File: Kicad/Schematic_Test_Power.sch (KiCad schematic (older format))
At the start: 16 parts, among them J201 Conn_02x01 BATTERY, SW201 SW_DIP_x01, U201 STBC08, U202 AP22811BW5, U203 TLV75528PDBV

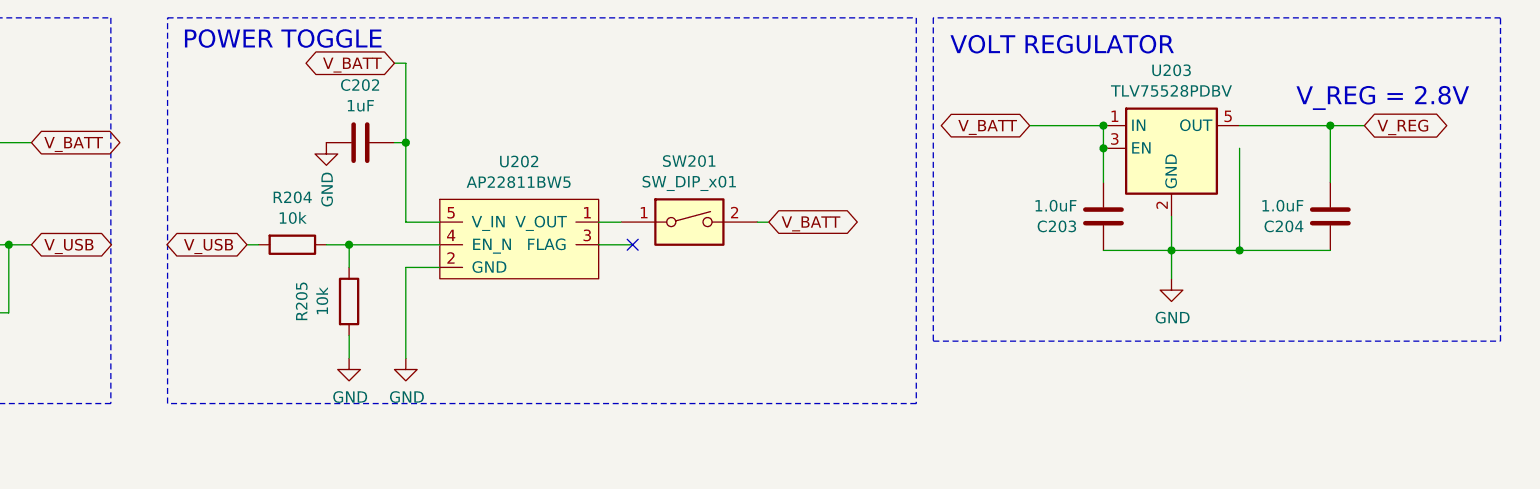
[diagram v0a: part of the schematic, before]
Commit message: Corrected some schematic labeling.
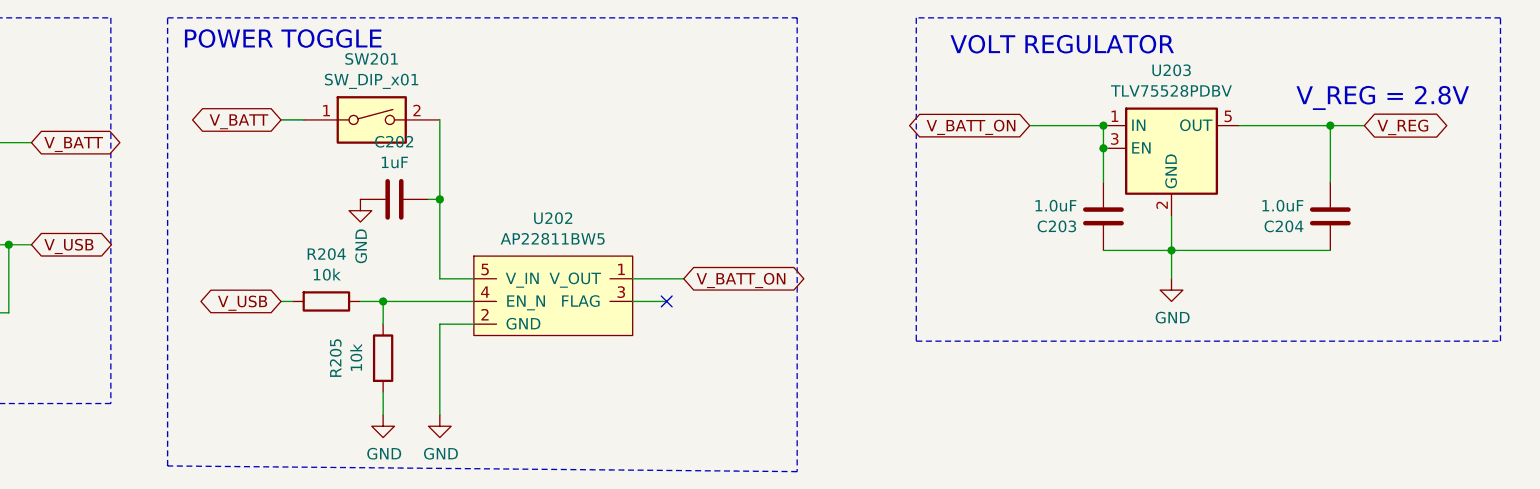
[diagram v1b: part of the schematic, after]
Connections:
- net GND: no longer U203.4 (NC)
- net V_BATT: now also SW201.1; no longer C202.1, C203.2, SW201.2, U202.5 (V_IN), U203.1 (IN), U203.3 (EN)
- net V_BATT_ON: now reaches U202.1 (V_OUT)
- net V_BATT_ON: now also C203.2, U203.1 (IN), U203.3 (EN); no longer SW201.1
- new net: C202.1, SW201.2, U202.5 (V_IN)
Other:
- moved on the sheet: C202, R204, R205, SW201, U202
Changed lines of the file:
@@
 L power:GND #PWR?
 U 1 1 5F6E4B62
-P 5725 3725
+P 5875 3975
 AR Path="/5F6E4B62" Ref="#PWR?"  Part="1"
 AR Path="/5F580D08/5F6E4B62" Ref="#PWR0207"  Part="1"
-F 0 "#PWR0207" H 5725 3475 50  0001 C CNN
-F 1 "GND" H 5730 3552 50  0000 C CNN
-F 2 "" H 5725 3725 50  0001 C CNN
-F 3 "" H 5725 3725 50  0001 C CNN
-	1    5725 3725
-	1    0    0    -1
-$EndComp
-Wire Wire Line
-	5725 3325 5725 3725
-Wire Wire Line
-	5875 3325 5725 3325
-Text GLabel 5675 2425 0    50   BiDi ~ 0
-V_BATT
+F 0 "#PWR0207" H 5875 3725 50  0001 C CNN
+F 1 "GND" H 5880 3802 50  0000 C CNN
+F 2 "" H 5875 3975 50  0001 C CNN
+F 3 "" H 5875 3975 50  0001 C CNN
+	1    5875 3975
+	1    0    0    -1
+$EndComp
+Wire Wire Line
+	5875 3575 5875 3975
+Wire Wire Line
+	6025 3575 5875 3575
 $Comp
 L StarGazer:AP22811BW5 U?
 U 1 1 5F6E4B6E
-P 6225 3025
+P 6375 3275
 AR Path="/5F6E4B6E" Ref="U?"  Part="1"
 AR Path="/5F580D08/5F6E4B6E" Ref="U202"  Part="1"
-F 0 "U202" H 6225 3190 50  0000 C CNN
-F 1 "AP22811BW5" H 6225 3099 50  0000 C CNN
-F 2 "Package_TO_SOT_SMD:TSOT-23-5_HandSoldering" H 6225 3075 50  0001 C CNN
-F 3 "" H 6225 3075 50  0001 C CNN
-F 4 "Mosfet, active low (batt protection)" H 6225 3025 50  0001 C CNN "part_details"
-F 5 " AP22811BW5-7 " H 6225 3025 50  0001 C CNN "part_name"
-F 6 "https://www.digikey.com/product-detail/en/diodes-incorporated/AP22811BW5-7/AP22811BW5-7DICT-ND/8545787" H 6225 3025 50  0001 C CNN "part_url"
-	1    6225 3025
+F 0 "U202" H 6375 3440 50  0000 C CNN
+F 1 "AP22811BW5" H 6375 3349 50  0000 C CNN
+F 2 "Package_TO_SOT_SMD:TSOT-23-5_HandSoldering" H 6375 3325 50  0001 C CNN
+F 3 "" H 6375 3325 50  0001 C CNN
+F 4 "Mosfet, active low (batt protection)" H 6375 3275 50  0001 C CNN "part_details"
+F 5 " AP22811BW5-7 " H 6375 3275 50  0001 C CNN "part_name"
+F 6 "https://www.digikey.com/product-detail/en/diodes-incorporated/AP22811BW5-7/AP22811BW5-7DICT-ND/8545787" H 6375 3275 50  0001 C CNN "part_url"
+	1    6375 3275
 	1    0    0    -1
 $EndComp
@@
 L Device:C C?
 U 1 1 5F6E4B74
-P 5525 2775
+P 5675 3025
 AR Path="/5F6E4B74" Ref="C?"  Part="1"
 AR Path="/5F580D08/5F6E4B74" Ref="C202"  Part="1"
-F 0 "C202" V 5273 2775 50  0000 C CNN
-F 1 "1uF" V 5364 2775 50  0000 C CNN
-F 2 "" H 5563 2625 50  0001 C CNN
-F 3 "~" H 5525 2775 50  0001 C CNN
-	1    5525 2775
+F 0 "C202" V 5423 3025 50  0000 C CNN
+F 1 "1uF" V 5514 3025 50  0000 C CNN
+F 2 "" H 5713 2875 50  0001 C CNN
+F 3 "~" H 5675 3025 50  0001 C CNN
+	1    5675 3025
 	0    1    1    0
 $EndComp
@@
 L power:GND #PWR?
 U 1 1 5F6E4B7A
-P 5375 2775
+P 5525 3025
 AR Path="/5F6E4B7A" Ref="#PWR?"  Part="1"
 AR Path="/5F580D08/5F6E4B7A" Ref="#PWR0205"  Part="1"
-F 0 "#PWR0205" H 5375 2525 50  0001 C CNN
-F 1 "GND" V 5380 2647 50  0000 R CNN
-F 2 "" H 5375 2775 50  0001 C CNN
-F 3 "" H 5375 2775 50  0001 C CNN
-	1    5375 2775
+F 0 "#PWR0205" H 5525 2775 50  0001 C CNN
+F 1 "GND" V 5530 2897 50  0000 R CNN
+F 2 "" H 5525 3025 50  0001 C CNN
+F 3 "" H 5525 3025 50  0001 C CNN
+	1    5525 3025
 	1    0    0    -1
 $EndComp
@@
 L Device:R R?
 U 1 1 5F6E4B84
-P 5475 3475
+P 5625 3725
 AR Path="/5F6E4B84" Ref="R?"  Part="1"
 AR Path="/5F580D08/5F6E4B84" Ref="R205"  Part="1"
-F 0 "R205" V 5268 3475 50  0000 C CNN
-F 1 "10k" V 5359 3475 50  0000 C CNN
-F 2 "Resistor_SMD:R_1206_3216Metric_Pad1.42x1.75mm_HandSolder" V 5405 3475 50  0001 C CNN
-F 3 "~" H 5475 3475 50  0001 C CNN
-F 4 "" H 5475 3475 50  0001 C CNN "Name"
-F 5 "" H 5475 3475 50  0001 C CNN "part_details"
-F 6 "Resistor - Pull Up" H 5475 3475 50  0001 C CNN "part_name"
-F 7 "https://www.digikey.com/product-detail/en/yageo/RC1206JR-0710KL/311-10KERCT-ND/732156" H 5475 3475 50  0001 C CNN "part_url"
-	1    5475 3475
-	1    0    0    -1
-$EndComp
-Wire Wire Line
-	5475 3625 5475 3725
+F 0 "R205" V 5418 3725 50  0000 C CNN
+F 1 "10k" V 5509 3725 50  0000 C CNN
+F 2 "Resistor_SMD:R_1206_3216Metric_Pad1.42x1.75mm_HandSolder" V 5555 3725 50  0001 C CNN
+F 3 "~" H 5625 3725 50  0001 C CNN
+F 4 "" H 5625 3725 50  0001 C CNN "Name"
+F 5 "" H 5625 3725 50  0001 C CNN "part_details"
+F 6 "Resistor - Pull Up" H 5625 3725 50  0001 C CNN "part_name"
+F 7 "https://www.digikey.com/product-detail/en/yageo/RC1206JR-0710KL/311-10KERCT-ND/732156" H 5625 3725 50  0001 C CNN "part_url"
+	1    5625 3725
+	1    0    0    -1
+$EndComp
+Wire Wire Line
+	5625 3875 5625 3975
 $Comp
 L power:GND #PWR?
 U 1 1 5F6E4B8B
-P 5475 3725
+P 5625 3975
 AR Path="/5F6E4B8B" Ref="#PWR?"  Part="1"
 AR Path="/5F580D08/5F6E4B8B" Ref="#PWR0206"  Part="1"
-F 0 "#PWR0206" H 5475 3475 50  0001 C CNN
-F 1 "GND" H 5480 3552 50  0000 C CNN
-F 2 "" H 5475 3725 50  0001 C CNN
-F 3 "" H 5475 3725 50  0001 C CNN
-	1    5475 3725
-	1    0    0    -1
-$EndComp
-Wire Wire Line
-	5475 3325 5475 3225
-Wire Wire Line
-	5475 3225 5875 3225
-Connection ~ 5475 3225
-Text GLabel 5025 3225 0    50   BiDi ~ 0
+F 0 "#PWR0206" H 5625 3725 50  0001 C CNN
+F 1 "GND" H 5630 3802 50  0000 C CNN
+F 2 "" H 5625 3975 50  0001 C CNN
+F 3 "" H 5625 3975 50  0001 C CNN
+	1    5625 3975
+	1    0    0    -1
+$EndComp
+Wire Wire Line
+	5625 3575 5625 3475
+Wire Wire Line
+	5625 3475 6025 3475
+Connection ~ 5625 3475
+Text GLabel 5175 3475 0    50   BiDi ~ 0
 V_USB
 Wire Wire Line
-	5075 3225 5025 3225
-Wire Wire Line
-	5375 3225 5475 3225
+	5225 3475 5175 3475
+Wire Wire Line
+	5525 3475 5625 3475
 $Comp
 L Device:R R?
 U 1 1 5F6E4B9B
-P 5225 3225
+P 5375 3475
 AR Path="/5F6E4B9B" Ref="R?"  Part="1"
 AR Path="/5F580D08/5F6E4B9B" Ref="R204"  Part="1"
-F 0 "R204" V 5018 3225 50  0000 C CNN
-F 1 "10k" V 5109 3225 50  0000 C CNN
-F 2 "Resistor_SMD:R_1206_3216Metric_Pad1.42x1.75mm_HandSolder" V 5155 3225 50  0001 C CNN
-F 3 "~" H 5225 3225 50  0001 C CNN
-F 4 "" H 5225 3225 50  0001 C CNN "Name"
-F 5 "" H 5225 3225 50  0001 C CNN "part_details"
-F 6 "Resistor - Pull Up" H 5225 3225 50  0001 C CNN "part_name"
-F 7 "https://www.digikey.com/product-detail/en/yageo/RC1206JR-0710KL/311-10KERCT-ND/732156" H 5225 3225 50  0001 C CNN "part_url"
-	1    5225 3225
+F 0 "R204" V 5168 3475 50  0000 C CNN
+F 1 "10k" V 5259 3475 50  0000 C CNN
+F 2 "Resistor_SMD:R_1206_3216Metric_Pad1.42x1.75mm_HandSolder" V 5305 3475 50  0001 C CNN
+F 3 "~" H 5375 3475 50  0001 C CNN
+F 4 "" H 5375 3475 50  0001 C CNN "Name"
+F 5 "" H 5375 3475 50  0001 C CNN "part_details"
+F 6 "Resistor - Pull Up" H 5375 3475 50  0001 C CNN "part_name"
+F 7 "https://www.digikey.com/product-detail/en/yageo/RC1206JR-0710KL/311-10KERCT-ND/732156" H 5375 3475 50  0001 C CNN "part_url"
+	1    5375 3475
 	0    1    1    0
 $EndComp
 Wire Wire Line
-	5725 3125 5875 3125
-Wire Wire Line
-	6575 3225 6725 3225
+	5875 3375 6025 3375
+Wire Wire Line
+	6725 3475 6875 3475
 Connection ~ 3075 2775
 Text Notes 3625 3775 2    50   ~ 0
@@
 Wire Notes Line
 	4425 3925 875  3925
-NoConn ~ 6725 3225
-Wire Wire Line
-	5675 2775 5725 2775
-Wire Wire Line
-	5725 2775 5725 3125
-Connection ~ 5725 2775
-Wire Wire Line
-	5725 2775 5725 2425
-Wire Wire Line
-	5725 2425 5675 2425
-Wire Notes Line
-	4675 3925 4675 2225
-Wire Notes Line
-	4675 2225 7975 2225
-Wire Notes Line
-	7975 2225 7975 3925
-Wire Notes Line
-	7975 3925 4675 3925
+NoConn ~ 6875 3475
+Wire Wire Line
+	5825 3025 5875 3025
+Wire Wire Line
+	5875 3025 5875 3375
+Connection ~ 5875 3025
+Wire Wire Line
+	5875 3025 5875 2675
+Wire Notes Line
+	4675 4200 4675 2225
+Wire Notes Line
+	4675 2225 7450 2225
+Wire Notes Line
+	7450 2225 7450 4225
+Wire Notes Line
+	7450 4225 4675 4200
 Text Notes 5625 2375 2    79   ~ 0
 POWER TOGGLE
@@
 L Switch:SW_DIP_x01 SW?
 U 1 1 5F6E4BB5
-P 6975 3125
+P 5575 2675
 AR Path="/5F6E4BB5" Ref="SW?"  Part="1"
 AR Path="/5F580D08/5F6E4BB5" Ref="SW201"  Part="1"
-F 0 "SW201" H 6975 3392 50  0000 C CNN
-F 1 "SW_DIP_x01" H 6975 3301 50  0000 C CNN
-F 2 "" H 6975 3125 50  0001 C CNN
-F 3 "~" H 6975 3125 50  0001 C CNN
-	1    6975 3125
-	1    0    0    -1
-$EndComp
-Wire Wire Line
-	6575 3125 6675 3125
-Wire Wire Line
-	7275 3125 7325 3125
+F 0 "SW201" H 5575 2942 50  0000 C CNN
+F 1 "SW_DIP_x01" H 5575 2851 50  0000 C CNN
+F 2 "" H 5575 2675 50  0001 C CNN
+F 3 "~" H 5575 2675 50  0001 C CNN
+	1    5575 2675
+	1    0    0    -1
+$EndComp
 Text GLabel 9950 2700 2    51   BiDi ~ 0
 V_REG
 Text Notes 8125 2400 0    79   ~ 0
 VOLT REGULATOR\n
-Text GLabel 7325 3125 2    50   BiDi ~ 0
-V_BATT
+Text GLabel 6950 3375 2    50   BiDi ~ 0
+V_BATT_ON
 Text GLabel 8475 2700 0    50   BiDi ~ 0
-V_BATT
+V_BATT_ON
 $Comp
 L Regulator_Linear:TLV75528PDBV U?
@@
 	9800 2700 9950 2700
 Wire Wire Line
-	9400 2800 9400 3250
-Connection ~ 9400 3250
-Wire Wire Line
-	9400 3250 9800 3250
-Wire Wire Line
 	8800 2950 8800 2800
-Wire Wire Line
-	9100 3250 9400 3250
 Wire Wire Line
 	9100 3100 9100 3250
@@
 V_REG = 2.8V\n
 Wire Notes Line
-	8050 2225 8050 3650
-Wire Notes Line
-	8050 3650 10550 3650
+	7975 2225 7975 3650
+Wire Notes Line
+	7975 3650 10550 3650
 Wire Notes Line
 	10550 3650 10550 2225
 Wire Notes Line
-	10550 2225 8050 2225
+	10550 2225 7975 2225
+Text GLabel 5175 2675 0    50   BiDi ~ 0
+V_BATT
+Wire Wire Line
+	5175 2675 5275 2675
+Wire Wire Line
+	6725 3375 6950 3375
+Wire Wire Line
+	9100 3250 9800 3250
 $EndSCHEMATC

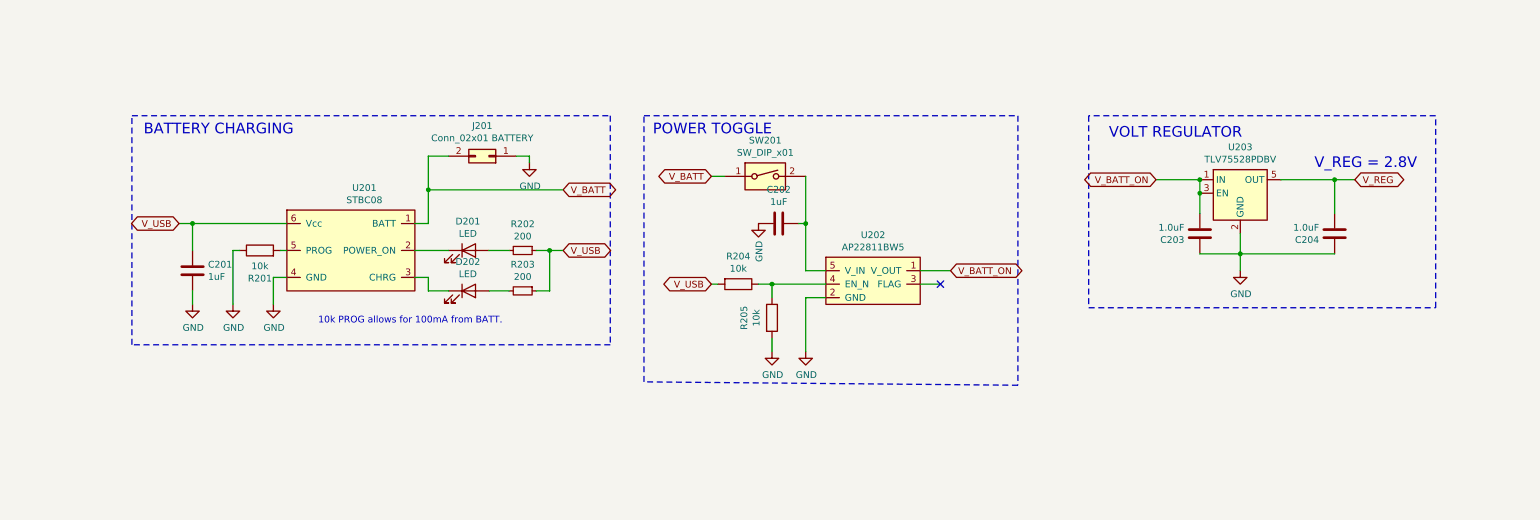
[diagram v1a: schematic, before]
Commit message: Assigned footprints to majority of refs. Missing is i2c due to unknown trace length.
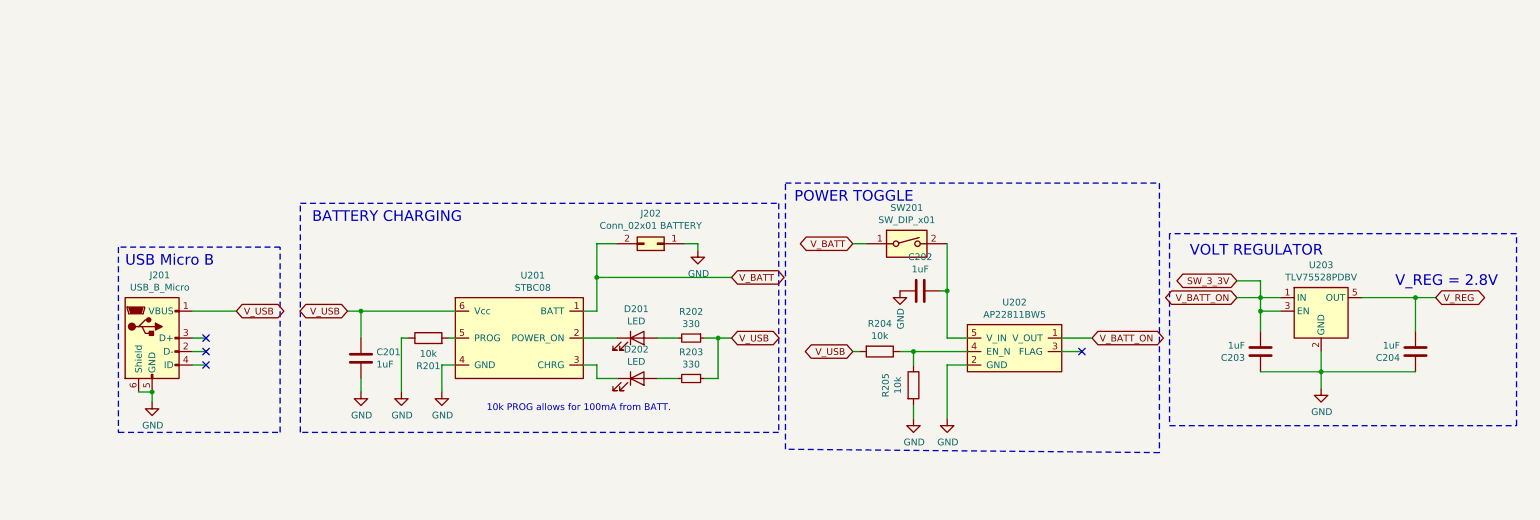
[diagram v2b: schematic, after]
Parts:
- added J201: USB_B_Micro, Connector_USB:USB_Micro-B_Amphenol_10103594-0001LF_Horizontal, symbol Connector:USB_B_Micro
- C201, C202: footprint (none) -> Capacitor_SMD:C_0805_2012Metric_Pad1.15x1.40mm_HandSolder; part_name (none) -> Capactitor - Bypass; part_url (none) -> https://www.digikey.com/product-detail/en/w%C3%BCrth-elektr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
- C203, C204: value 1.0uF -> 1uF; footprint (none) -> Capacitor_SMD:C_0805_2012Metric_Pad1.15x1.40mm_HandSolder; part_name (none) -> Capactitor - Bypass; part_url (none) -> https://www.digikey.com/product-detail/en/w%C3%BCrth-elektr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
- D201: footprint (none) -> Diode_SMD:D_1206_3216Metric; part_details (none) -> RED when ERROR; part_name (none) -> LED - Red; part_url (none) -> https://www.digikey.com/product-detail/en/w%C3%BCrth-elektr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
- D202: footprint (none) -> Diode_SMD:D_1206_3216Metric; part_details (none) -> GREEN when CHARGING; part_name (none) -> LED - Green; part_url (none) -> https://www.digikey.com/product-detail/en/w%C3%BCrth-elektr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
- J202: renamed from J201; footprint (none) -> Connector_JST:JST_EH_B2B-EH-A_1x02_P2.50mm_Vertical; part_details (none) -> JST - 2 pin; part_url (none) -> LOCAL STOCK
- R202, R203: value 200 -> 330; part_url https://www.digikey.com/product-detail/en/yageo/RC1206FR-07200RL/311-200FRCT-ND/731622 -> https://www.digikey.com/product-detail/en/yageo/RC1206FR-07330RL/311-330FRCT-ND/731769
- SW201: footprint (none) -> Connector_JST:JST_EH_B2B-EH-A_1x02_P2.50mm_Vertical; part_details (none) -> JST - 2 pin (switch attached to case); part_name (none) -> Switch - Power; part_url (none) -> https://www.amazon.com/MTS-101-Position-Miniature-Toggle-Sw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
- U201: footprint (none) -> Package_DFN_QFN:DFN-6-1EP_3x3mm_P0.95mm_EP1.7x2.6mm
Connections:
- net GND: now also J201.5 (GND), J201.6 (Shield)
- net V_USB: now also J201.1 (VBUS)
- net V_BATT_ON renamed SW_3_3V
- no-connect marks 1 -> 4
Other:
- note added: "USB Micro B\n"
- moved on the sheet: C201, C202, C203, C204, D201, D202, J202, R201, R202, R203, R204, R205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

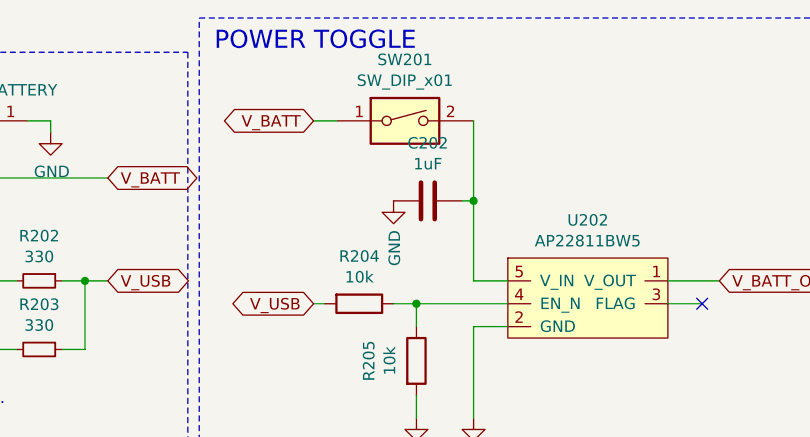
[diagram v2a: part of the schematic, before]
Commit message: Many parts are now placed on PCB.
Work left off on MC, gyro, and mag.

Discovered free-angle mode for traces, which will make connections look better in the future.
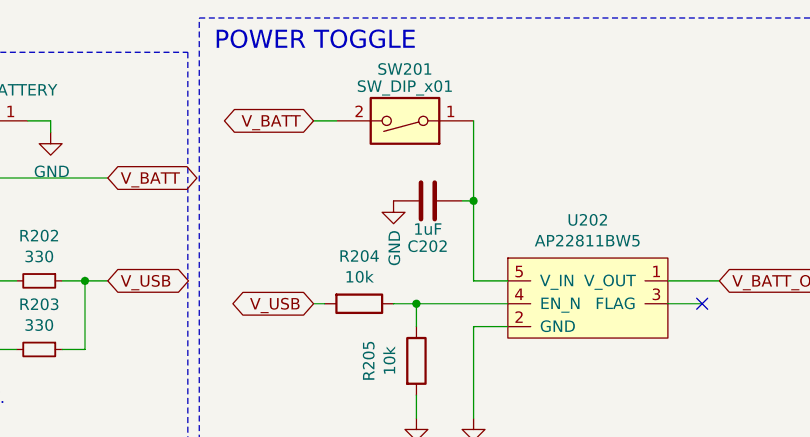
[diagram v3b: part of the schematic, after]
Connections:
- net V_BATT: now also SW201.2; no longer SW201.1
- net at C202.1, U202.5 (V_IN): now also SW201.1; no longer SW201.2
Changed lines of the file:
@@
 AR Path="/5F6E4B74" Ref="C?"  Part="1"
 AR Path="/5F580D08/5F6E4B74" Ref="C202"  Part="1"
-F 0 "C202" V 6473 3525 50  0000 C CNN
-F 1 "1uF" V 6564 3525 50  0000 C CNN
+F 0 "C202" V 6925 3525 50  0000 C CNN
+F 1 "1uF" V 6850 3525 50  0000 C CNN
 F 2 "Capacitor_SMD:C_0805_2012Metric_Pad1.15x1.40mm_HandSolder" H 6763 3375 50  0001 C CNN
 F 3 "~" H 6725 3525 50  0001 C CNN
@@
 AR Path="/5F6E4BB5" Ref="SW?"  Part="1"
 AR Path="/5F580D08/5F6E4BB5" Ref="SW201"  Part="1"
-F 0 "SW201" H 6625 3442 50  0000 C CNN
-F 1 "SW_DIP_x01" H 6625 3351 50  0000 C CNN
+F 0 "SW201" H 6625 2950 50  0000 C CNN
+F 1 "SW_DIP_x01" H 6625 3025 50  0000 C CNN
 F 2 "Connector_JST:JST_EH_B2B-EH-A_1x02_P2.50mm_Vertical" H 6625 3175 50  0001 C CNN
 F 3 "~" H 6625 3175 50  0001 C CNN
@@
 F 6 "https://www.amazon.com/MTS-101-Position-Miniature-Toggle-Switch/dp/B0799LBFNY/ref=lp_306596011_1_8?s=industrial&ie=UTF8&qid=1599516393&sr=1-8" H 6625 3175 50  0001 C CNN "part_url"
 	1    6625 3175
-	1    0    0    -1
+	-1   0    0    1
 $EndComp
 Text GLabel 10550 3575 2    51   BiDi ~ 0
